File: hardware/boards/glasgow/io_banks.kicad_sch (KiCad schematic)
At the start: 27 parts, among them J10 AUX, J4 Conn_01x02, J5 PinHeader_2x22_P1.27mm, U30 ICE40HX8K-BG121, U32 SN74LVC1T45DCKR

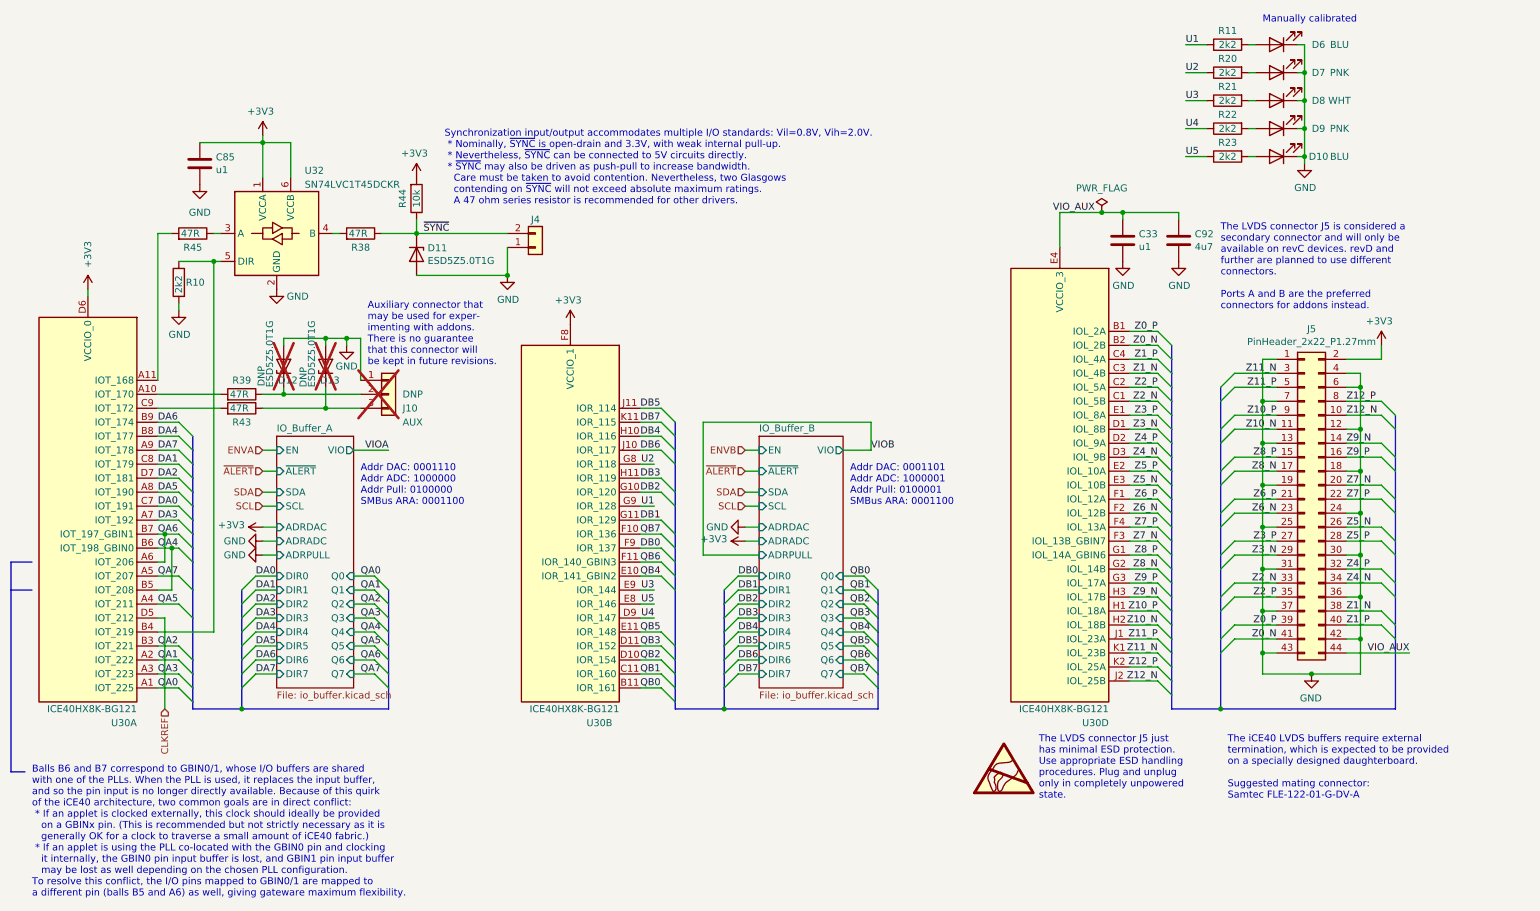
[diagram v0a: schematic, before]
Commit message: Remove one of the sides
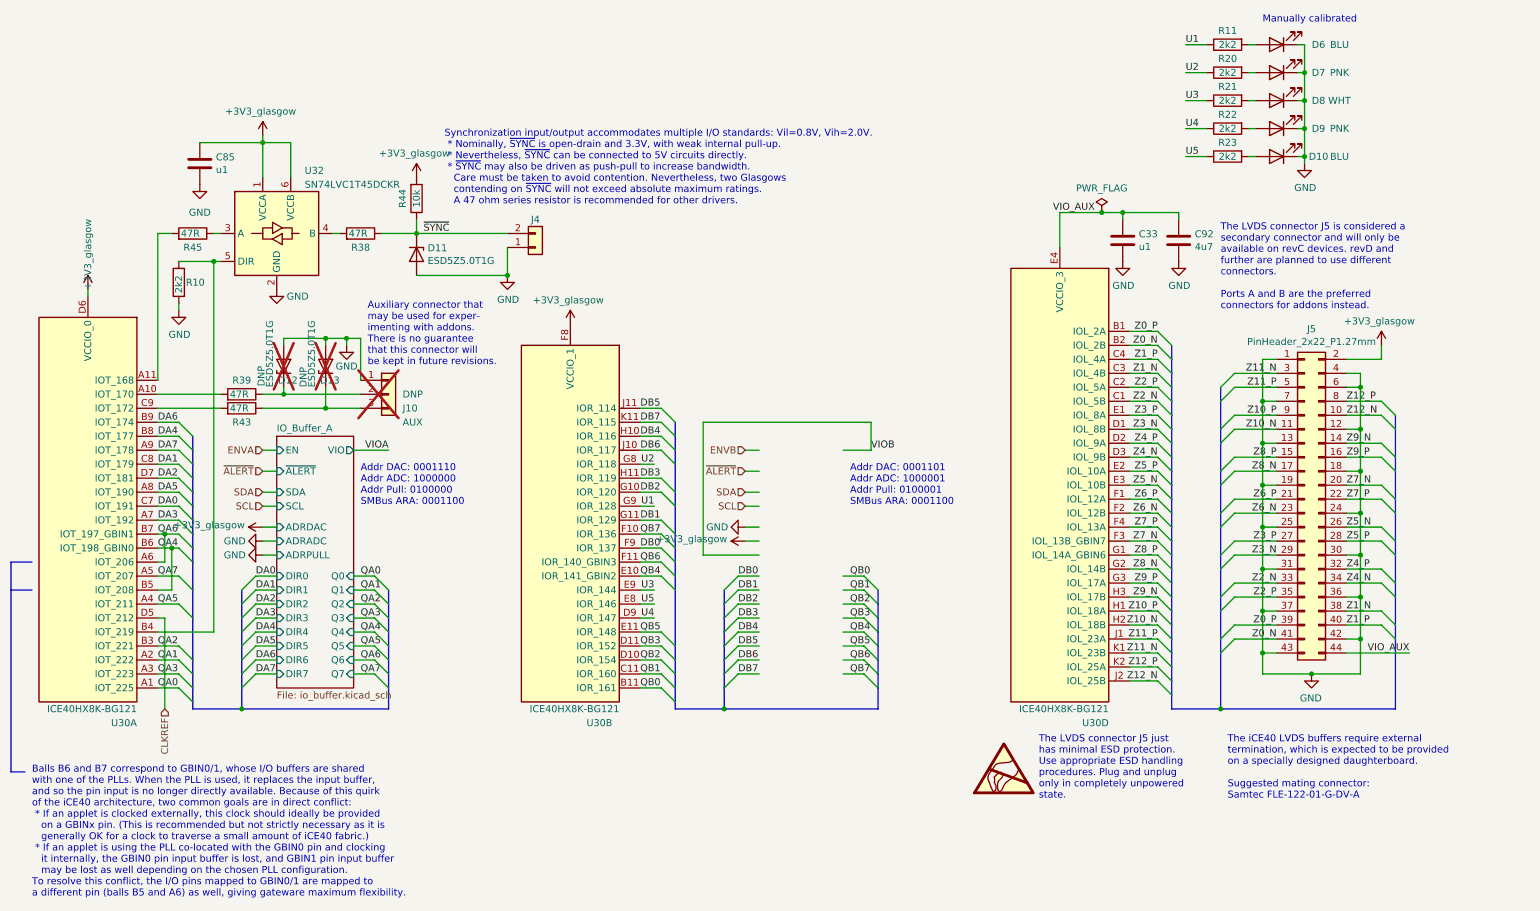
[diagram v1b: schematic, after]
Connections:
- net +3V3 renamed +3V3_glasgow
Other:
- removed sheet IO_Buffer_B
